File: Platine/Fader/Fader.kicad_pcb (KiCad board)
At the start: 2 copper layers, 9 parts, among them J1 FaderPWR, J2 FaderSignal, J3 Motor13Out, J4 Motor4Out, J5 Conn_01x19, J6 Conn_01x19, U1 MC12, U3 MC34, U4 YAAJ_DCDC_StepDown_LM2596

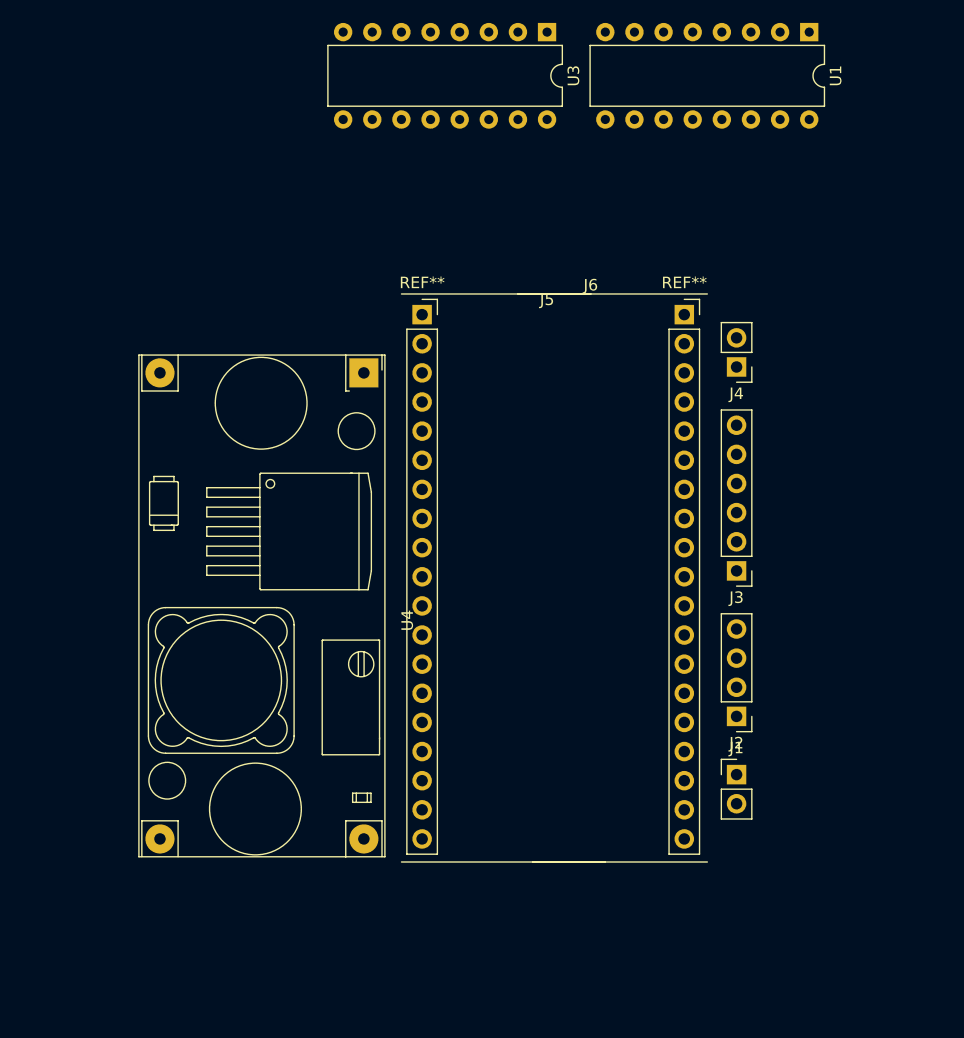
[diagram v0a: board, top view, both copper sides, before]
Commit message: Rearranged pcb schematic. Added first traces and coorect ESP32 footprint model
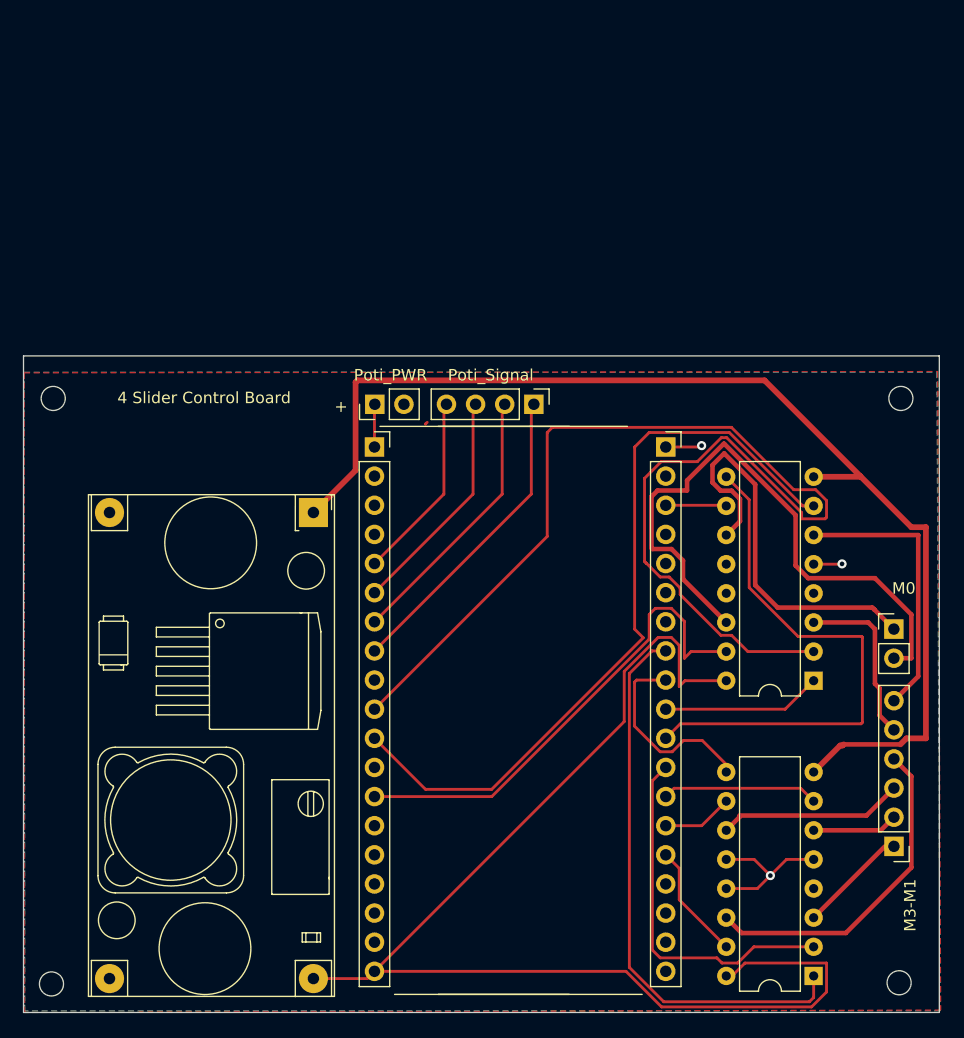
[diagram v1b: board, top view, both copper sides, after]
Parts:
- removed J5: Conn_01x19, fp_esp32_dev4:esp32_dev_left
- removed J6: Conn_01x19, fp_esp32_dev4:esp32_dev4_right
- added  : MountingHole_2.1mm, MountingHole:MountingHole_2.1mm, F.Cu at (29.3, 99.3)
- added  : ESp32Gesamt, ESp32Gesamt, F.Cu at (63.0, 122.0)
- added  : MountingHole_2.1mm, MountingHole:MountingHole_2.1mm, F.Cu at (103.2, 99.3)
- added  : esp32_38_pins-custom_library, Library:ESP32, F.Cu at (70.0, 101.0)
- added  : MountingHole_2.1mm, MountingHole:MountingHole_2.1mm, F.Cu at (103.1, 150.2)
- added  : MountingHole_2.1mm, MountingHole:MountingHole_2.1mm, F.Cu at (29.2, 150.3)
-  : renamed from J4
-  : renamed from U4
-  : renamed from U1
-  : renamed from J1
-  : renamed from J3
-  : renamed from U3
-  : renamed from J2
- moved   82.3 mm to (95.6, 149.6), turned to 180 degrees
- moved   61.1 mm to (95.6, 123.9), turned to 180 degrees
- moved   45.1 mm to (57.4, 99.8), turned to 90 degrees
- moved   32.5 mm to (71.2, 99.8), turned to -90 degrees
- moved   27.7 mm to (102.6, 138.3)
- moved   26.7 mm to (102.6, 119.4), turned to 0 degrees
- moved   12.9 mm to (52.0, 109.2)
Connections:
-   pad 1: Net-(U3-Pad11) -> Net-(J4-Pad1)
-   pad 2: Net-(U3-Pad14) -> Net-(J4-Pad2)
-   pad 4: GND -> (no net) (x2)
-   pad 1: Net-(U1-Pad3) -> Net-(J3-Pad1)
-   pad 2: Net-(U1-Pad6) -> Net-(J3-Pad2)
-   pad 3: Net-(U1-Pad11) -> Net-(J3-Pad3)
-   pad 4: Net-(U1-Pad14) -> Net-(J3-Pad4)
-   pad 5: Net-(U3-Pad3) -> Net-(J3-Pad5)
-   pad 6: Net-(U3-Pad6) -> Net-(J3-Pad6)
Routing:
- net VCCQ: track 0.00 -> 107.9 mm
- net Net-(U2-Pad26): track 0.00 -> 105.2 mm
- net /VCCM: track 0.00 -> 101.7 mm
- net Net-(U2-Pad27): track 0.00 -> 66.5 mm
- net Net-(J4-Pad2): track 0.00 -> 53.8 mm
- net Net-(U1-PadEN1,2): track 0.00 -> 49.0 mm
- net Net-(U2-Pad17): track 0.00 -> 47.3 mm
- net Net-(U2-Pad12): track 0.00 -> 42.7 mm
- net Net-(J4-Pad1): track 0.00 -> 35.9 mm
- net Net-(U1-PadI1): track 0.00 -> 31.5 mm
- net Net-(J3-Pad4): track 0.00 -> 29.2 mm
- net Net-(J2-Pad1): track 0.00 -> 26.9 mm
- net Net-(J3-Pad6): track 0.00 -> 24.4 mm
- net Net-(J2-Pad2): track 0.00 -> 23.4 mm
- net Net-(J2-Pad3): track 0.00 -> 19.8 mm
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- added copper zone on B.Cu, net GND
- added copper zone on F.Cu, net GND
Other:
- board outline added: 79.9 x 57.3 mm
- board text added: "+"
- board text added: "4 Slider Control Board"
- board text added: "M0"
- board text added: "M3-M1"
- board text added: "Poti_PWR"
- board text added: "Poti_Signal"

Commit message: Connect Slider Touch Pins to ESP32 touch sensitive pins
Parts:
- added  : FaderTouch, Connector_PinHeader_2.54mm:PinHeader_1x04_P2.54mm_Vertical, F.Cu at (83.2, 99.7)
- U1: renamed from  
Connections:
-   pad 13: unconnected-(U2-Pad13) -> Net-(U2-Pad13)
-   pad 14: unconnected-(U2-Pad14) -> Net-(U2-Pad14)
-   pad 32: Net-(J2-Pad2) -> Net-(U2-Pad32)
-   pad 33: Net-(J2-Pad1) -> Net-(U2-Pad33)
-   pad 34: Net-(J2-Pad4) -> Net-(J2-Pad2)
-   pad 35: Net-(J2-Pad3) -> Net-(J2-Pad1)
-   pad SN: unconnected-(U2-PadSN) -> Net-(J2-Pad3)
-   pad SP: unconnected-(U2-PadSP) -> Net-(J2-Pad4)
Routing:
- net Net-(U2-Pad13): track 0.00 -> 57.6 mm
- net Net-(U2-Pad14): track 0.00 -> 46.0 mm
- net Net-(U2-Pad33): track 0.00 -> 30.9 mm
- net Net-(U2-Pad32): track 0.00 -> 26.7 mm
- net Net-(U3-PadI1): track 105.2 -> 100.4 mm
- net Net-(J2-Pad3): track 19.8 -> 15.0 mm
- net Net-(J2-Pad1): track 26.9 -> 22.2 mm
- net Net-(J2-Pad4): track 16.2 -> 11.4 mm
- net Net-(J2-Pad2): track 23.4 -> 18.6 mm
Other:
- board text added: "Slider_Touch"
